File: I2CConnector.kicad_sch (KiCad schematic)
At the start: 13 parts, among them J6 I2C, Q5 Q_NMOS_GSD, Q6 Q_NMOS_GSD

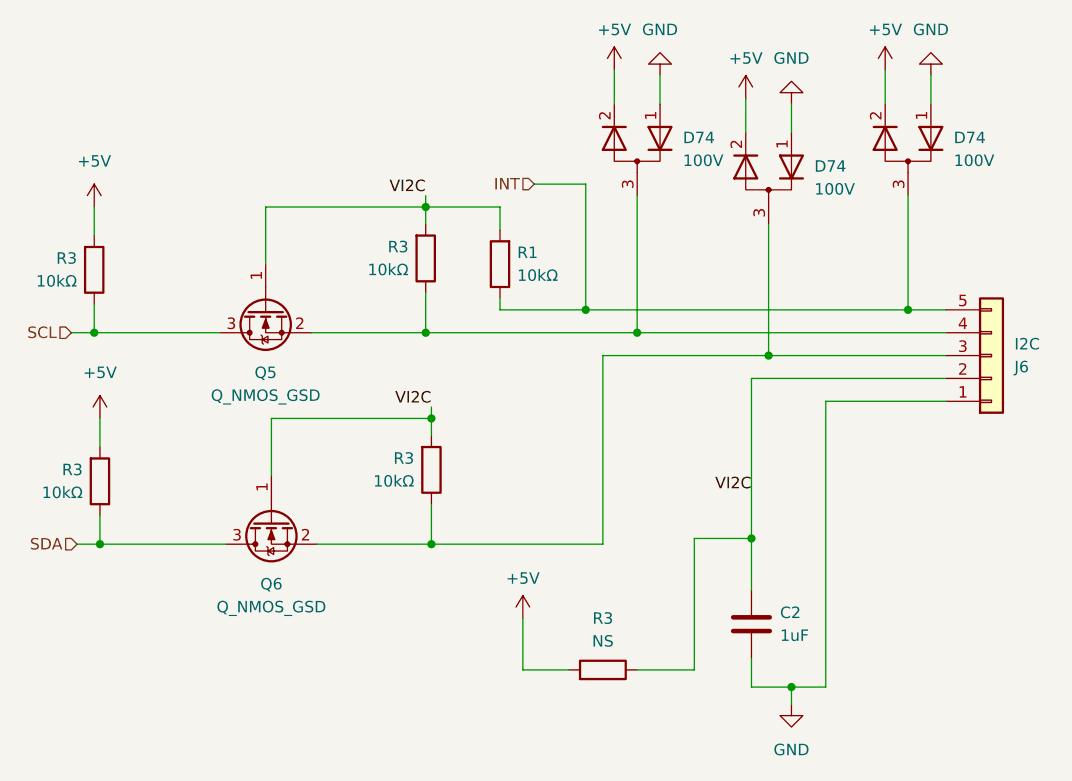
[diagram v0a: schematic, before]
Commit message: Updated gate driver to BD6222 since the old one did not have enough current.
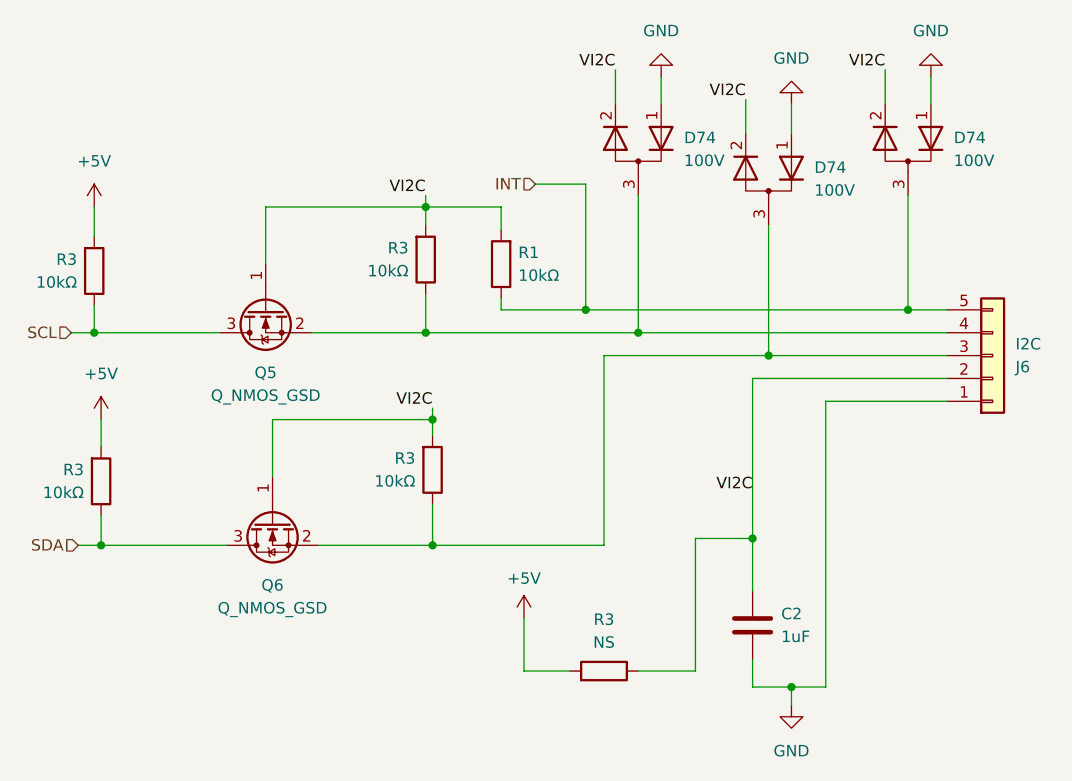
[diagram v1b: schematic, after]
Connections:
- net +5V: no longer D74.2 (K), D74.2 (K), D74.2 (K)
- net VI2C: now also D74.2 (K), D74.2 (K), D74.2 (K)
